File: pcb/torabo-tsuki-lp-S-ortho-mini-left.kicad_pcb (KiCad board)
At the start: 2 copper layers, 138.8 x 74 mm, 59 parts, among them J101 FTSH-106-01-L-D-K, SW10 SW_Push, SW11 SW_Push, SW12 SW_Push, SW13 SW_Push, SW15 SW_Push, SW16 SW_Push, SW17 SW_Push, SW18 SW_Push, SW19 SW_Push, SW20 SW_Push, SW22 SW_Push, SW23 SW_Push, SW24 SW_Push, SW25 SW_Push, SW26 SW_Push, SW27 SW_Push, SW28 SW_Push, SW29 SW_Push, SW30 SW_Push, SW31 SW_Push, SW32 SW_Push, SW33 SW_Push, SW34 SW_Push, SW35 SW_Push, SW8 SW_Push, SW9 SW_Push

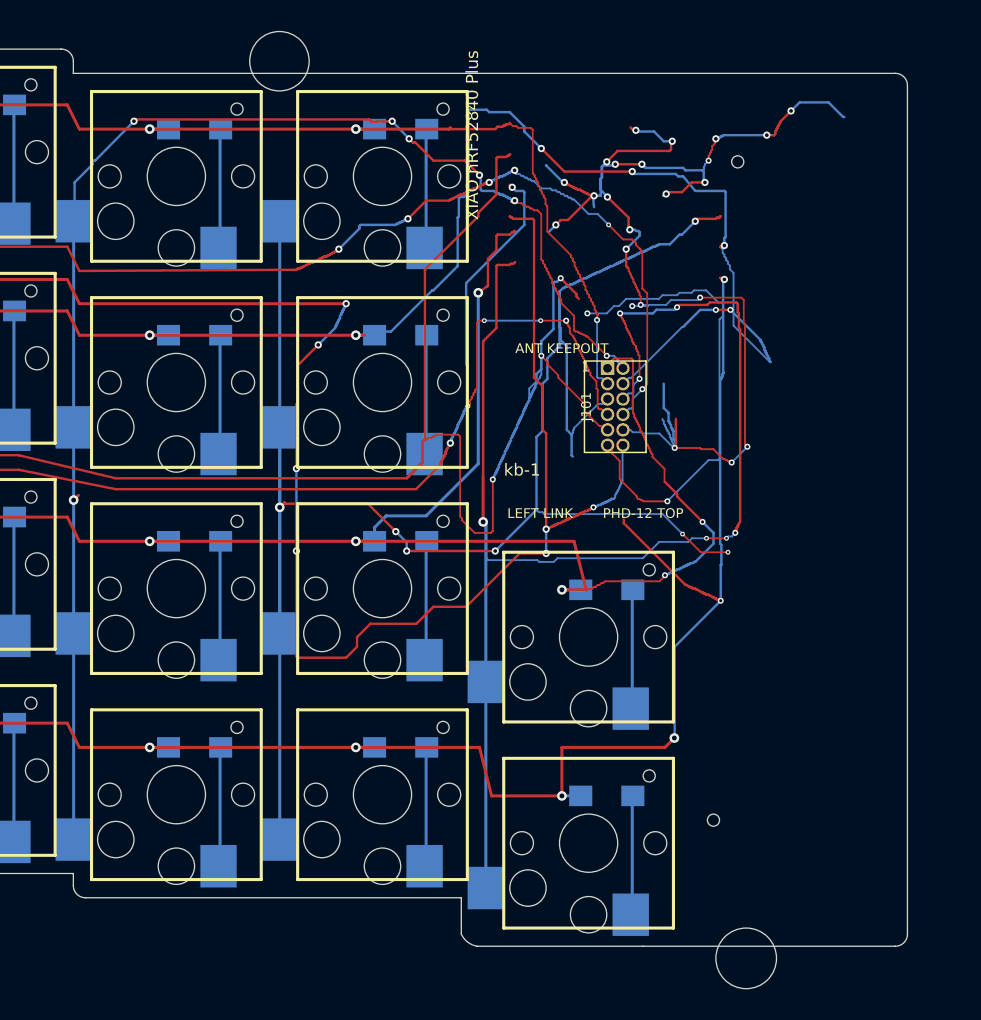
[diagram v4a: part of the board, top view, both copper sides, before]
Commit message: Shrink inner edges of split PCBs
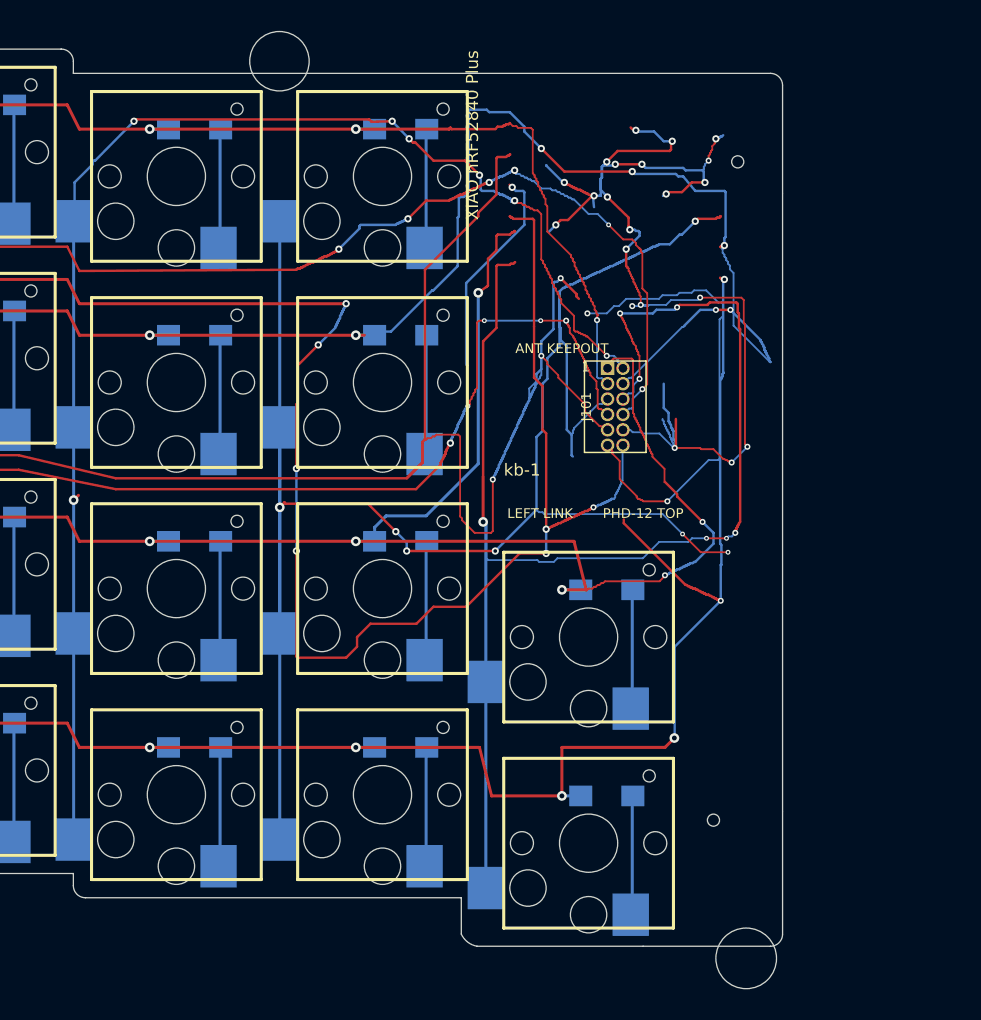
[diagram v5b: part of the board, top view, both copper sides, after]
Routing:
- net GND: track 114.6 -> 102.6 mm, vias 23 -> 21
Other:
- board size 138.8 x 74 mm -> 128.5 x 74 mm
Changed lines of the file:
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@@
 	(gr_line
 		(start 78.5 42.5)
-		(end 146.3 42.5)
+		(end 136 42.5)
 		(stroke
 			(width 0.1)
@@
 	)
 	(gr_arc
-		(start 146.3 42.5)
-		(mid 147.007107 42.792893)
-		(end 147.3 43.5)
+		(start 136 42.5)
+		(mid 136.707107 42.792893)
+		(end 137 43.5)
 		(stroke
 			(width 0.1)
@@
 	)
 	(gr_line
-		(start 146.3 114.5)
+		(start 136 114.5)
 		(end 125.5 114.5)
 		(stroke
@@
 	)
 	(gr_line
-		(start 147.3 43.5)
-		(end 147.3 52.4)
+		(start 137 43.5)
+		(end 137 52.4)
 		(stroke
 			(width 0.1)
@@
 	)
 	(gr_line
-		(start 147.3 52.4)
-		(end 147.3 103.4)
+		(start 137 52.4)
+		(end 137 103.4)
 		(stroke
 			(width 0.1)
@@
 	)
 	(gr_line
-		(start 147.3 103.4)
-		(end 147.3 113.5)
+		(start 137 103.4)
+		(end 137 113.5)
 		(stroke
 			(width 0.1)
@@
 	)
 	(gr_arc
-		(start 147.3 113.5)
-		(mid 147.007107 114.207107)
-		(end 146.3 114.5)
+		(start 137 113.5)
+		(mid 136.707107 114.207107)
+		(end 136 114.5)
 		(stroke
 			(width 0.1)
@@
 	)
 	(segment
-		(start 136.6 47)
-		(end 136.5 47.1)
-		(width 0.2)
-		(layer "F.Cu")
-		(net "GND")
-	)
-	(segment
 		(start 124.8 59.8)
 		(end 124.7 59.7)
@@
 	)
 	(segment
-		(start 136.8 46.5)
-		(end 136.8 46.6)
-		(width 0.2)
-		(layer "F.Cu")
-		(net "GND")
-	)
-	(segment
 		(start 120.4 52.2)
 		(end 120.5 52.2)
@@
 	)
 	(segment
-		(start 136.7 46.8)
-		(end 136.6 46.9)
-		(width 0.2)
-		(layer "F.Cu")
-		(net "GND")
-	)
-	(segment
 		(start 120.1 52.1)
 		(end 120.3 52.1)
@@
 	)
 	(segment
-		(start 136.4 47.5)
-		(end 136.3 47.6)
-		(width 0.2)
-		(layer "F.Cu")
-		(net "GND")
-	)
-	(segment
 		(start 124.8 59.9)
 		(end 124.8 59.8)
@@
 	)
 	(segment
-		(start 136.5 47.2)
-		(end 136.4 47.3)
-		(width 0.2)
-		(layer "F.Cu")
-		(net "GND")
-	)
-	(segment
 		(start 120.7 52.3)
 		(end 120.8 52.4)
@@
 	)
 	(segment
-		(start 136.275 47.6)
-		(end 135.7 47.6)
-		(width 0.2)
-		(layer "F.Cu")
-		(net "GND")
-	)
-	(segment
 		(start 132.1 74.3)
 		(end 132.199999 74.3)
@@
 	)
 	(segment
-		(start 136.3 47.6)
-		(end 136.275 47.6)
-		(width 0.2)
-		(layer "F.Cu")
-		(net "GND")
-	)
-	(segment
 		(start 120 52)
 		(end 120.1 52.1)
@@
 	)
 	(segment
-		(start 136.5 47.1)
-		(end 136.5 47.2)
-		(width 0.2)
-		(layer "F.Cu")
-		(net "GND")
-	)
-	(segment
 		(start 132.5 74.5)
 		(end 132.699999 74.5)
@@
 	)
 	(segment
-		(start 136.7 46.7)
-		(end 136.7 46.8)
-		(width 0.2)
-		(layer "F.Cu")
-		(net "GND")
-	)
-	(segment
 		(start 120.5 52.2)
 		(end 120.6 52.3)
@@
 	)
 	(segment
-		(start 136.8 46.6)
-		(end 136.7 46.7)
-		(width 0.2)
-		(layer "F.Cu")
-		(net "GND")
-	)
-	(segment
 		(start 119.4 51.7)
 		(end 119.5 51.8)
@@
 	)
 	(segment
-		(start 136.4 47.3)
-		(end 136.4 47.5)
-		(width 0.2)
-		(layer "F.Cu")
-		(net "GND")
-	)
-	(segment
 		(start 119.6 51.8)
 		(end 119.7 51.9)
@@
 	)
 	(segment
-		(start 136.6 46.9)
-		(end 136.6 47)
-		(width 0.2)
-		(layer "F.Cu")
-		(net "GND")
-	)
-	(segment
 		(start 124.6 47.1)
 		(end 124.5 47)
@@
 		(net "GND")
 	)
-	(segment
-		(start 137.7 45.6)
-		(end 136.8 46.5)
-		(width 0.2)
-		(layer "F.Cu")
-		(net "GND")
-	)
 	(via
 		(at 128.099999 73.4)
@@
 	)
 	(via
-		(at 135.7 47.6)
-		(size 0.6)
-		(drill 0.3)
-		(layers "F.Cu" "B.Cu")
-		(net "GND")
-	)
-	(via
 		(at 124.1 57)
 		(size 0.6)
@@
 	)
 	(via
-		(at 137.7 45.6)
-		(size 0.6)
-		(drill 0.3)
-		(layers "F.Cu" "B.Cu")
-		(net "GND")
-	)
-	(via
 		(at 127.4 52.45)
 		(size 0.6)
@@
 	)
 	(segment
-		(start 142.1 46.1)
-		(end 142 46.1)
-		(width 0.2)
-		(layer "B.Cu")
-		(net "GND")
-	)
-	(segment
 		(start 121.3 52.6)
 		(end 121.35 52.6)
@@
 	)
 	(segment
-		(start 140.8 44.9)
-		(end 138.4 44.9)
-		(width 0.2)
-		(layer "B.Cu")
-		(net "GND")
-	)
-	(segment
 		(start 130.5 50.4)
 		(end 130.4 50.5)
@@
 	)
 	(segment
-		(start 135.7 47.6)
-		(end 132.1 47.6)
-		(width 0.2)
-		(layer "B.Cu")
-		(net "GND")
-	)
-	(segment
 		(start 130.9 49.7)
 		(end 130.6 50)
@@
 	)
 	(segment
-		(start 142 46.1)
-		(end 140.8 44.9)
-		(width 0.2)
-		(layer "B.Cu")
-		(net "GND")
-	)
-	(segment
 		(start 117.725 55.6)
 		(end 117.7 55.6)
@@
 		(width 0.2)
 		(layer "B.Cu")
-		(net "GND")
-	)
-	(segment
-		(start 138.4 44.9)
-		(end 137.7 45.6)
-		(width 0.2)
-		(layer "B.Cu")

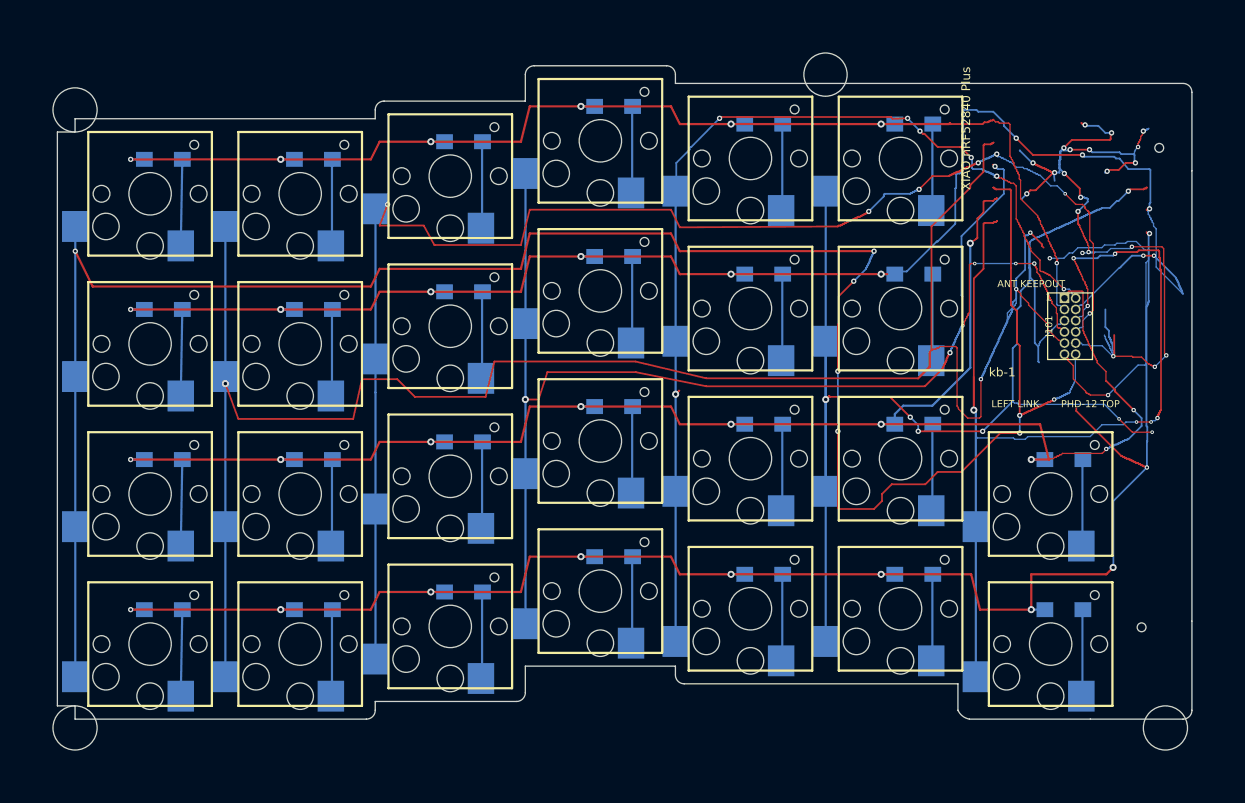
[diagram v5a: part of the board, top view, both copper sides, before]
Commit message: Add routed screw reliefs to both PCBs and panel
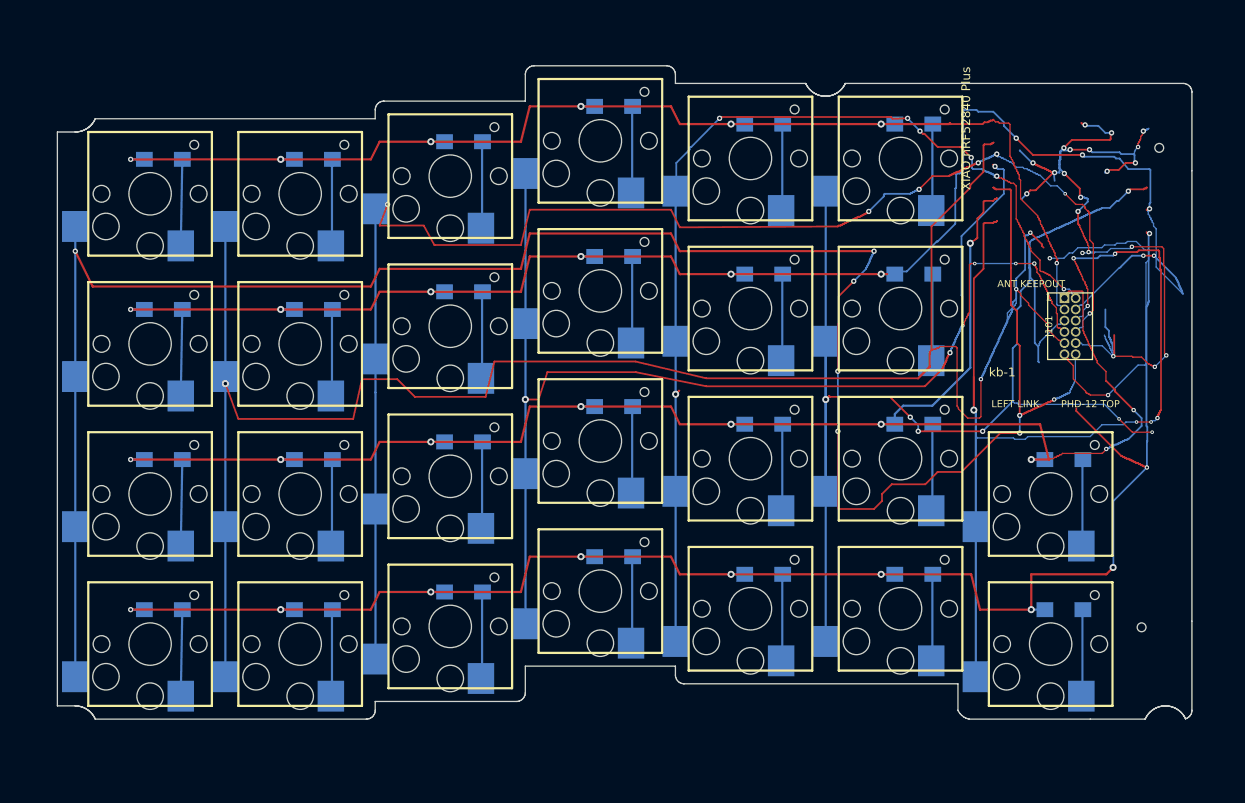
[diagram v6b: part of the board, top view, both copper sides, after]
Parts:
- removed the REF** at (95.5, 41.5)
- removed the REF** at (10.5, 45.5)
- removed the REF** at (134.0, 115.5)
- removed the REF** at (10.5, 115.5)
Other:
- outline, holes or cut-outs redrawn

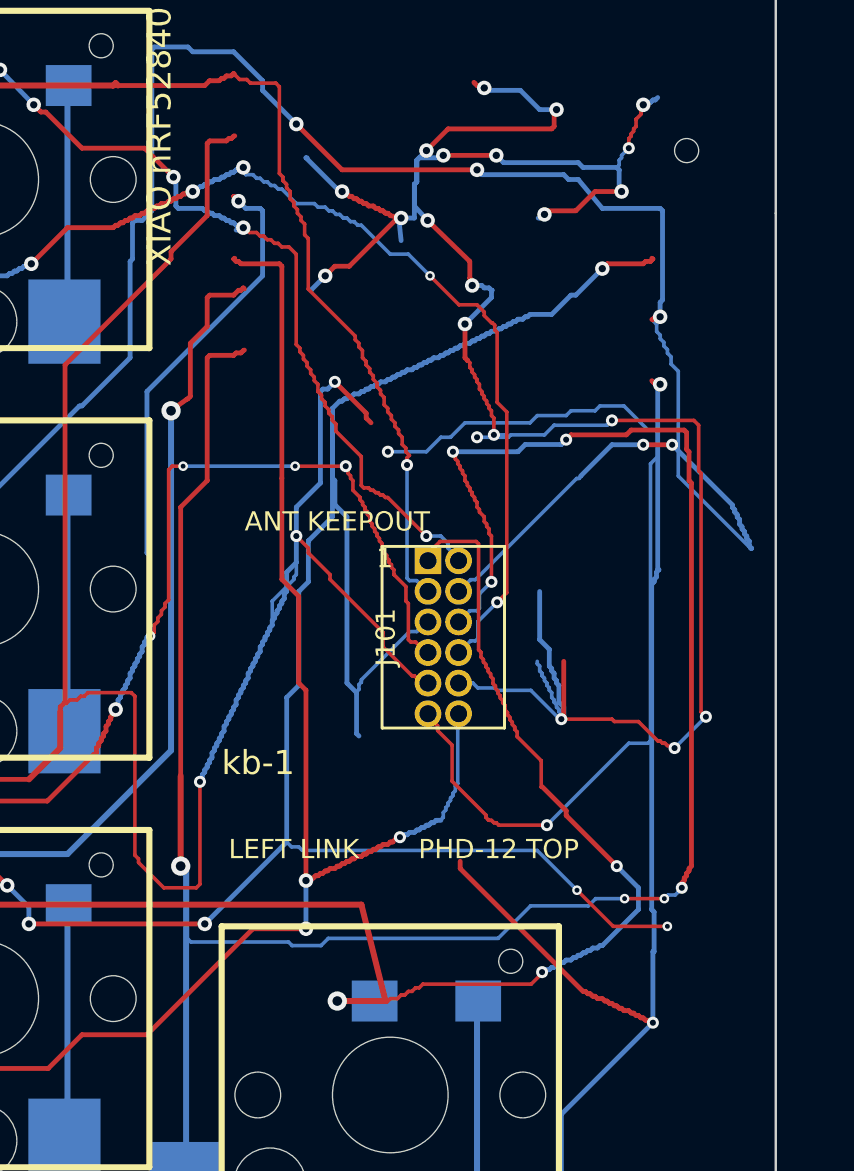
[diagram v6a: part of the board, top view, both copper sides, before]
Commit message: Use standard 0.3 mm vias for JLCPCB panels
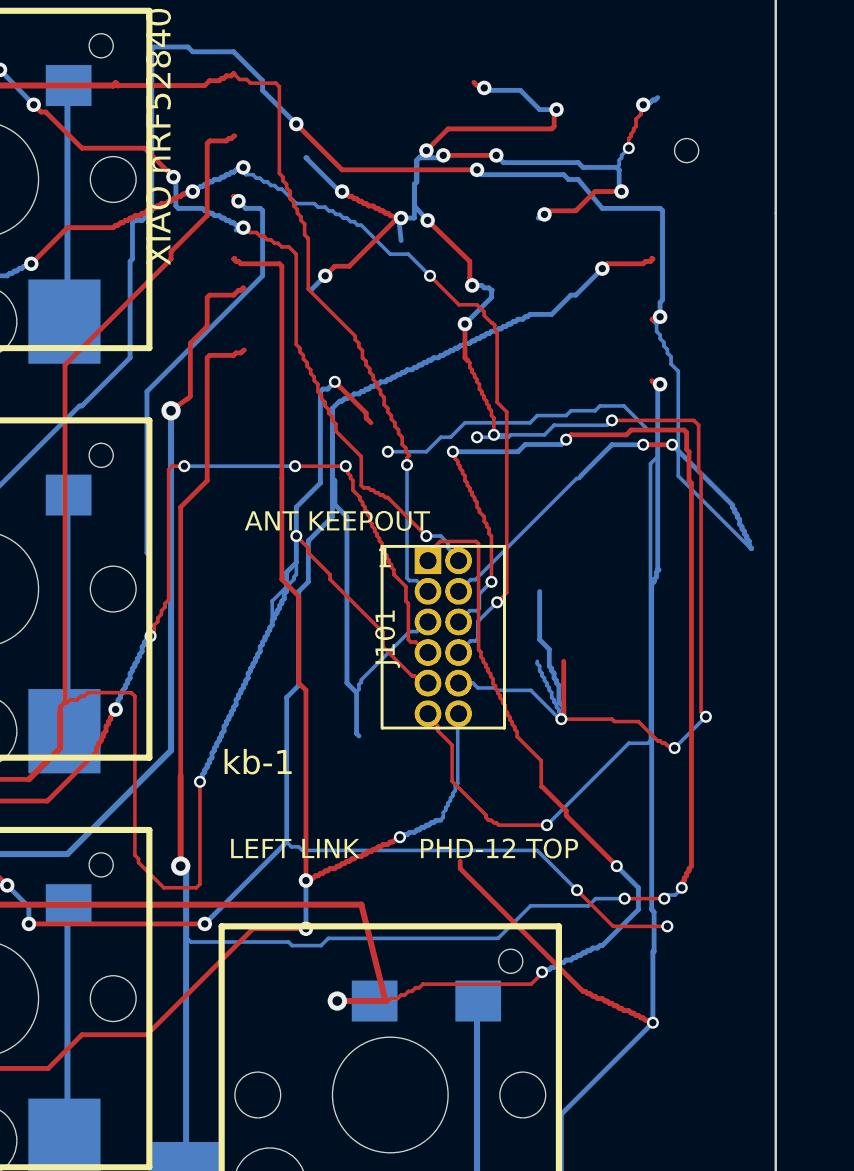
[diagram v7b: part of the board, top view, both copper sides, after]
